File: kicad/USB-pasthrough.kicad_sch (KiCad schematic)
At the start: 93 parts, among them J1 USB_Power, J2 USB_C, J3 Cortex Debug, J4 Power_Sel, J5 SPI Display, J6 SWD, J7 USB_A, J8 MicroSD, SW1 Boot0, SW2 Reset, U1 AMS1117, U2 STM32F723VET6, Y1 8 MHz

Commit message: Tweak ID names, add serial port
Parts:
- added J?: Serial, Connector_PinHeader_2.54mm:PinHeader_1x03_P2.54mm_Vertical, symbol Connector_Generic:Conn_01x03
- renumbered ID5 to ID0, ID4 to ID1, ID3 to ID2, ID2 to ID3, ID1 to ID4
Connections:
- net GND: now also J?.3 (Pin_3)
- net TXD: now reaches U2.24 (PA2)
- net TXD: now also J?.1 (Pin_1)
- net RXD: now reaches U2.25 (PA3)
- net RXD: now also J?.2 (Pin_2)
- no-connect marks 49 -> 47
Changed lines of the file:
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@@
   (no_connect (at 132.08 160.02))
   (no_connect (at 181.61 105.41))
-  (no_connect (at 132.08 68.58))
   (no_connect (at 81.28 109.22))
   (no_connect (at 81.28 137.16))
   (no_connect (at 81.28 157.48))
-  (no_connect (at 132.08 66.04))
   (no_connect (at 81.28 134.62))
   (no_connect (at 81.28 142.24))
@@
     (effects (font (size 1.27 1.27)) (justify left bottom))
   )
+  (label "RXD" (at 163.83 144.78 180)
+    (effects (font (size 1.27 1.27)) (justify right bottom))
+  )
   (label "MMC1_CLK" (at 132.08 177.8 0)
     (effects (font (size 1.27 1.27)) (justify left bottom))
@@
     (effects (font (size 1.27 1.27)) (justify left bottom))
   )
+  (label "TXD" (at 132.08 66.04 0)
+    (effects (font (size 1.27 1.27)) (justify left bottom))
+  )
   (label "MMC1_CDET" (at 50.8 96.52 0)
     (effects (font (size 1.27 1.27)) (justify left bottom))
@@
     (effects (font (size 1.27 1.27)) (justify left bottom))
   )
+  (label "RXD" (at 132.08 68.58 0)
+    (effects (font (size 1.27 1.27)) (justify left bottom))
+  )
   (label "SWO" (at 184.15 93.98 180)
     (effects (font (size 1.27 1.27)) (justify right bottom))
@@
     (effects (font (size 1.27 1.27)) (justify right bottom))
   )
+  (label "TXD" (at 163.83 142.24 180)
+    (effects (font (size 1.27 1.27)) (justify right bottom))
+  )
   (label "USBC-" (at 207.01 149.86 180)
     (effects (font (size 1.27 1.27)) (justify right bottom))
@@
   (symbol (lib_id "Jumper:Jumper_2_Open") (at 76.2 121.92 0) (mirror y) (unit 1)
     (in_bom yes) (on_board yes)
-    (property "Reference" "ID4" (id 0) (at 76.2 120.65 0))
+    (property "Reference" "ID1" (id 0) (at 76.2 120.65 0))
     (property "Value" "Jumper_2_Bridged" (id 1) (at 76.2 118.11 0)
       (effects (font (size 1.27 1.27)) hide)
@@
   (symbol (lib_id "Jumper:Jumper_2_Bridged") (at 76.2 119.38 0) (mirror y) (unit 1)
     (in_bom yes) (on_board yes)
-    (property "Reference" "ID5" (id 0) (at 76.2 118.11 0))
+    (property "Reference" "ID0" (id 0) (at 76.2 118.11 0))
     (property "Value" "Jumper_2_Bridged" (id 1) (at 76.2 115.57 0)
       (effects (font (size 1.27 1.27)) hide)
@@
     (pin "99")
   )
+  (symbol (lib_id "power:GND") (at 163.83 147.32 0) (unit 1)
+    (in_bom yes) (on_board yes)
+    (property "Reference" "#PWR?" (id 0) (at 163.83 153.67 0)
+      (effects (font (size 1.27 1.27)) hide)
+    )
+    (property "Value" "GND" (id 1) (at 160.02 148.59 0))
+    (property "Footprint" "" (id 2) (at 163.83 147.32 0)
+      (effects (font (size 1.27 1.27)) hide)
+    )
+    (property "Datasheet" "" (id 3) (at 163.83 147.32 0)
+      (effects (font (size 1.27 1.27)) hide)
+    )
+    (pin "1")
+  )
   (symbol (lib_id "power:GND") (at 160.02 60.96 0) (unit 1)
     (in_bom yes) (on_board yes)
@@
     (pin "2")
   )
+  (symbol (lib_id "Connector_Generic:Conn_01x03") (at 168.91 144.78 0) (unit 1)
+    (in_bom yes) (on_board yes) (fields_autoplaced)
+    (property "Reference" "J?" (id 0) (at 171.45 143.5099 0)
+      (effects (font (size 1.27 1.27)) (justify left))
+    )
+    (property "Value" "Serial" (id 1) (at 171.45 146.0499 0)
+      (effects (font (size 1.27 1.27)) (justify left))
+    )
+    (property "Footprint" "Connector_PinHeader_2.54mm:PinHeader_1x03_P2.54mm_Vertical" (id 2) (at 168.91 144.78 0)
+      (effects (font (size 1.27 1.27)) hide)
+    )
+    (property "Datasheet" "~" (id 3) (at 168.91 144.78 0)
+      (effects (font (size 1.27 1.27)) hide)
+    )
+    (pin "1")
+    (pin "2")
+    (pin "3")
+  )
   (symbol (lib_id "power:PWR_FLAG") (at 45.72 27.94 0) (unit 1)
     (in_bom yes) (on_board yes) (fields_autoplaced)
@@
   (symbol (lib_id "Jumper:Jumper_2_Bridged") (at 76.2 127 0) (mirror y) (unit 1)
     (in_bom yes) (on_board yes)
-    (property "Reference" "ID2" (id 0) (at 76.2 125.73 0))
+    (property "Reference" "ID3" (id 0) (at 76.2 125.73 0))
     (property "Value" "Jumper_2_Bridged" (id 1) (at 76.2 123.19 0)
       (effects (font (size 1.27 1.27)) hide)
@@
   (symbol (lib_id "Jumper:Jumper_2_Bridged") (at 76.2 124.46 0) (mirror y) (unit 1)
     (in_bom yes) (on_board yes)
-    (property "Reference" "ID3" (id 0) (at 76.2 123.19 0))
+    (property "Reference" "ID2" (id 0) (at 76.2 123.19 0))
     (property "Value" "Jumper_2_Bridged" (id 1) (at 76.2 120.65 0)
       (effects (font (size 1.27 1.27)) hide)
@@
   (symbol (lib_id "Jumper:Jumper_2_Bridged") (at 76.2 129.54 0) (mirror y) (unit 1)
     (in_bom yes) (on_board yes)
-    (property "Reference" "ID1" (id 0) (at 76.2 128.27 0))
+    (property "Reference" "ID4" (id 0) (at 76.2 128.27 0))
     (property "Value" "Jumper_2_Bridged" (id 1) (at 76.2 125.73 0)
       (effects (font (size 1.27 1.27)) hide)
@@
       (reference "#PWR0108") (unit 1) (value "GND") (footprint "")
     )
+    (path "/2bf153cc-e448-4386-8752-8ba0ab506fbf"
+      (reference "#PWR?") (unit 1) (value "GND") (footprint "")
+    )
     (path "/17fb6d59-e121-4e89-9918-78c9648a257a"
       (reference "C1") (unit 1) (value "10uF") (footprint "Capacitor_THT:CP_Radial_D5.0mm_P2.50mm")
@@
       (reference "H4") (unit 1) (value "MountingHole") (footprint "MountingHole:MountingHole_2.2mm_M2_Pad")
     )
-    (path "/95c1312c-0851-4fe5-a936-d7533c7cbaf8"
-      (reference "ID1") (unit 1) (value "Jumper_2_Bridged") (footprint "Jumper:SolderJumper-2_P1.3mm_Bridged_Pad1.0x1.5mm")
+    (path "/1858f103-0550-4454-a9a8-cb3c44998e1e"
+      (reference "ID0") (unit 1) (value "Jumper_2_Bridged") (footprint "Jumper:SolderJumper-2_P1.3mm_Bridged_Pad1.0x1.5mm")
     )
-    (path "/8b9373f4-2597-4d9f-8245-62eb92cb212f"
-      (reference "ID2") (unit 1) (value "Jumper_2_Bridged") (footprint "Jumper:SolderJumper-2_P1.3mm_Bridged_Pad1.0x1.5mm")
+    (path "/1586b523-a3cf-43e8-bf9d-0533c598fcc1"
+      (reference "ID1") (unit 1) (value "Jumper_2_Bridged") (footprint "Jumper:SolderJumper-2_P1.3mm_Open_Pad1.0x1.5mm")
     )
     (path "/8d554622-7ff9-41d4-a107-16b60e1fce82"
-      (reference "ID3") (unit 1) (value "Jumper_2_Bridged") (footprint "Jumper:SolderJumper-2_P1.3mm_Bridged_Pad1.0x1.5mm")
+      (reference "ID2") (unit 1) (value "Jumper_2_Bridged") (footprint "Jumper:SolderJumper-2_P1.3mm_Bridged_Pad1.0x1.5mm")
     )
-    (path "/1586b523-a3cf-43e8-bf9d-0533c598fcc1"
-      (reference "ID4") (unit 1) (value "Jumper_2_Bridged") (footprint "Jumper:SolderJumper-2_P1.3mm_Open_Pad1.0x1.5mm")
+    (path "/8b9373f4-2597-4d9f-8245-62eb92cb212f"
+      (reference "ID3") (unit 1) (value "Jumper_2_Bridged") (footprint "Jumper:SolderJumper-2_P1.3mm_Bridged_Pad1.0x1.5mm")
     )
-    (path "/1858f103-0550-4454-a9a8-cb3c44998e1e"
-      (reference "ID5") (unit 1) (value "Jumper_2_Bridged") (footprint "Jumper:SolderJumper-2_P1.3mm_Bridged_Pad1.0x1.5mm")
+    (path "/95c1312c-0851-4fe5-a936-d7533c7cbaf8"
+      (reference "ID4") (unit 1) (value "Jumper_2_Bridged") (footprint "Jumper:SolderJumper-2_P1.3mm_Bridged_Pad1.0x1.5mm")
     )
     (path "/7cf7e8fc-d4c5-4161-b905-d74139026239"
@@
       (reference "J8") (unit 1) (value "MicroSD") (footprint "Connector_Card:microSD_HC_Hirose_DM3AT-SF-PEJM5")
     )
+    (path "/5e2d672b-5bf9-4abe-ba7e-647e105a370c"
+      (reference "J?") (unit 1) (value "Serial") (footprint "Connector_PinHeader_2.54mm:PinHeader_1x03_P2.54mm_Vertical")
+    )
     (path "/97339053-1ba0-429b-8e6a-4e4aa25ddc74"

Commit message: Start switching to Full Sized SD socket
The uSD socket is too small, use bigger socket for easier
soldering.
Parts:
- added J?: SD_Card, symbol Connector:SD_Card
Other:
- moved on the sheet: J?
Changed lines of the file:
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@@
     (effects (font (size 1.27 1.27)) (justify left bottom))
   )
-  (label "RXD" (at 163.83 144.78 180)
+  (label "RXD" (at 30.48 133.35 180)
     (effects (font (size 1.27 1.27)) (justify right bottom))
   )
@@
     (effects (font (size 1.27 1.27)) (justify right bottom))
   )
-  (label "TXD" (at 163.83 142.24 180)
+  (label "TXD" (at 30.48 130.81 180)
     (effects (font (size 1.27 1.27)) (justify right bottom))
   )
@@
     (pin "99")
   )
-  (symbol (lib_id "power:GND") (at 163.83 147.32 0) (unit 1)
+  (symbol (lib_id "power:GND") (at 30.48 135.89 0) (unit 1)
     (in_bom yes) (on_board yes)
-    (property "Reference" "#PWR?" (id 0) (at 163.83 153.67 0)
+    (property "Reference" "#PWR?" (id 0) (at 30.48 142.24 0)
       (effects (font (size 1.27 1.27)) hide)
     )
-    (property "Value" "GND" (id 1) (at 160.02 148.59 0))
-    (property "Footprint" "" (id 2) (at 163.83 147.32 0)
+    (property "Value" "GND" (id 1) (at 26.67 137.16 0))
+    (property "Footprint" "" (id 2) (at 30.48 135.89 0)
       (effects (font (size 1.27 1.27)) hide)
     )
-    (property "Datasheet" "" (id 3) (at 163.83 147.32 0)
+    (property "Datasheet" "" (id 3) (at 30.48 135.89 0)
       (effects (font (size 1.27 1.27)) hide)
     )
@@
     (pin "2")
   )
-  (symbol (lib_id "Connector_Generic:Conn_01x03") (at 168.91 144.78 0) (unit 1)
+  (symbol (lib_id "Connector_Generic:Conn_01x03") (at 35.56 133.35 0) (unit 1)
     (in_bom yes) (on_board yes) (fields_autoplaced)
-    (property "Reference" "J?" (id 0) (at 171.45 143.5099 0)
+    (property "Reference" "J?" (id 0) (at 38.1 132.0799 0)
       (effects (font (size 1.27 1.27)) (justify left))
     )
-    (property "Value" "Serial" (id 1) (at 171.45 146.0499 0)
+    (property "Value" "Serial" (id 1) (at 38.1 134.6199 0)
       (effects (font (size 1.27 1.27)) (justify left))
     )
-    (property "Footprint" "Connector_PinHeader_2.54mm:PinHeader_1x03_P2.54mm_Vertical" (id 2) (at 168.91 144.78 0)
+    (property "Footprint" "Connector_PinHeader_2.54mm:PinHeader_1x03_P2.54mm_Vertical" (id 2) (at 35.56 133.35 0)
       (effects (font (size 1.27 1.27)) hide)
     )
-    (property "Datasheet" "~" (id 3) (at 168.91 144.78 0)
+    (property "Datasheet" "~" (id 3) (at 35.56 133.35 0)
       (effects (font (size 1.27 1.27)) hide)
     )
@@
     (pin "2")
   )
+  (symbol (lib_id "Connector:SD_Card") (at 168.91 143.51 0) (unit 1)
+    (in_bom yes) (on_board yes) (fields_autoplaced)
+    (property "Reference" "J?" (id 0) (at 168.91 125.73 0))
+    (property "Value" "SD_Card" (id 1) (at 168.91 128.27 0))
+    (property "Footprint" "" (id 2) (at 168.91 143.51 0)
+      (effects (font (size 1.27 1.27)) hide)
+    )
+    (property "Datasheet" "http://portal.fciconnect.com/Comergent//fci/drawing/10067847.pdf" (id 3) (at 168.91 143.51 0)
+      (effects (font (size 1.27 1.27)) hide)
+    )
+    (pin "1")
+    (pin "10")
+    (pin "11")
+    (pin "12")
+    (pin "13")
+    (pin "2")
+    (pin "3")
+    (pin "4")
+    (pin "5")
+    (pin "6")
+    (pin "7")
+    (pin "8")
+    (pin "9")
+  )
   (symbol (lib_name "MountingHole_3") (lib_id "Mechanical:MountingHole") (at 20.32 80.01 0) (unit 1)
     (in_bom yes) (on_board yes) (fields_autoplaced)
@@
       (reference "J?") (unit 1) (value "Serial") (footprint "Connector_PinHeader_2.54mm:PinHeader_1x03_P2.54mm_Vertical")
     )
+    (path "/aa5a7d34-f533-44f1-a357-de5c629aef10"
+      (reference "J?") (unit 1) (value "SD_Card") (footprint "")
+    )
     (path "/97339053-1ba0-429b-8e6a-4e4aa25ddc74"

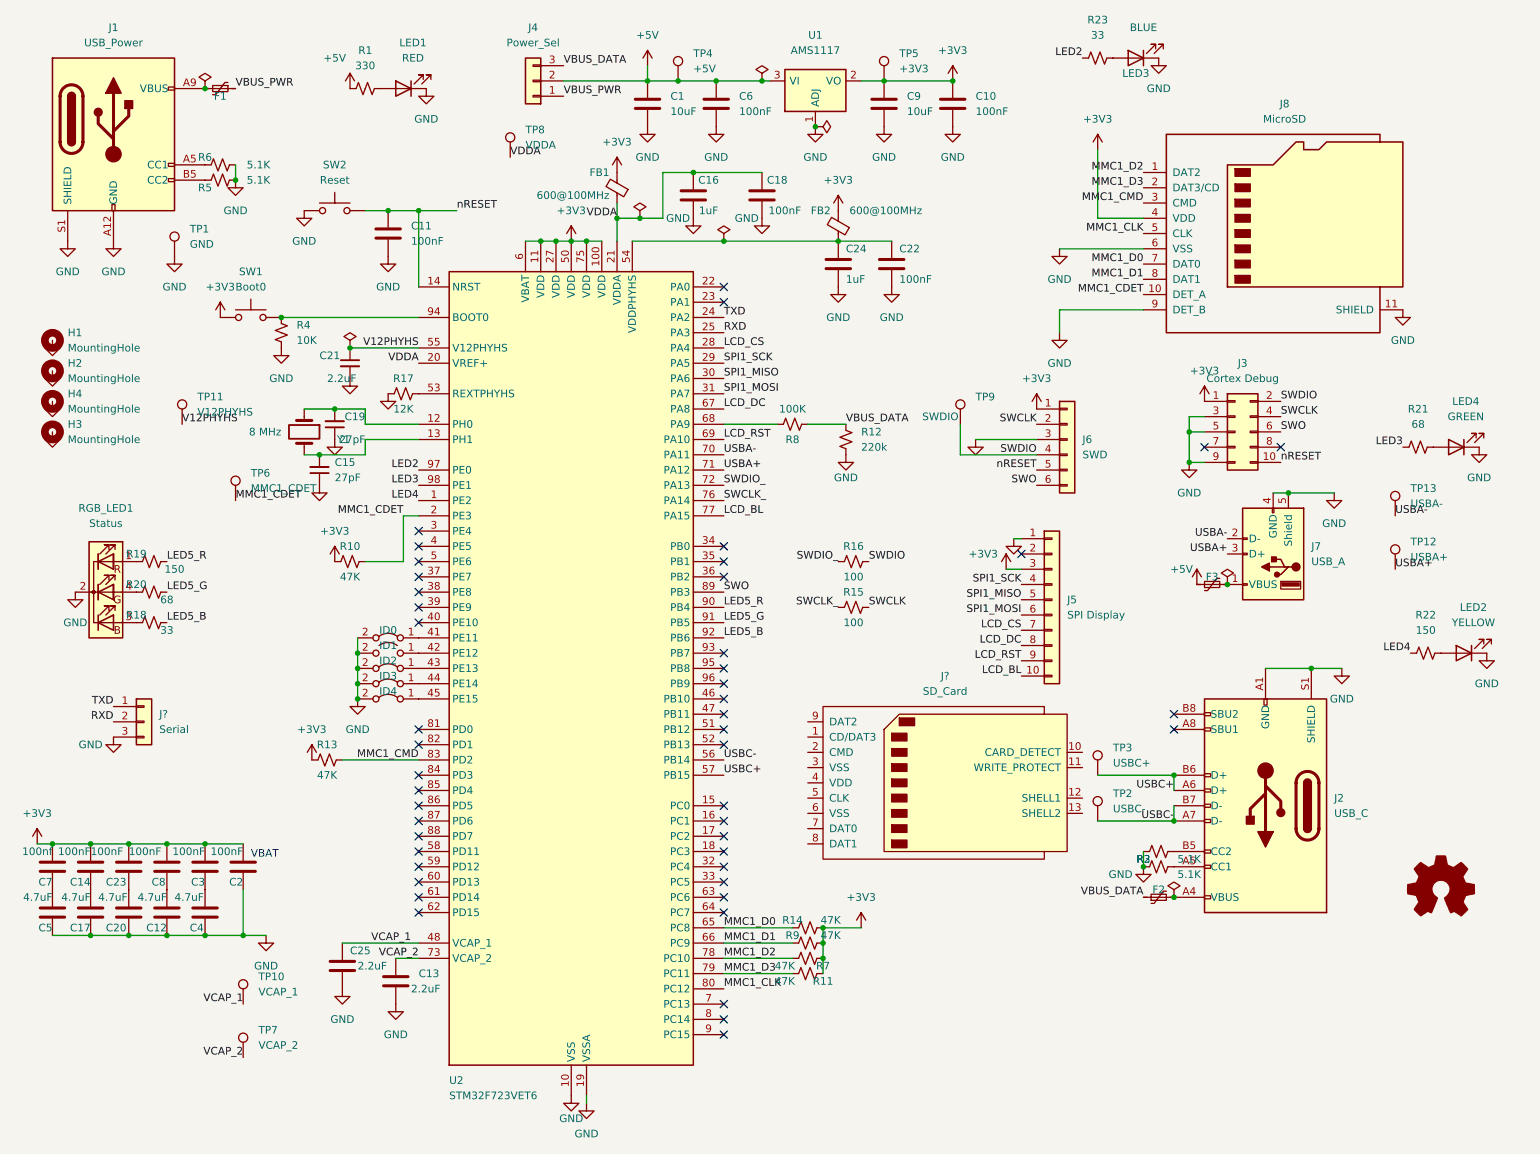
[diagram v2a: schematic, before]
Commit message: Add fulsized SD Card connector serial etc...
Add KiCad symbol and footprint for SD Card connector to try out
overlaying Full size and uSD connectors allowing support for either
one depending on which connector is installed.

Also add SMD USB A connector for possible use in place of THT.
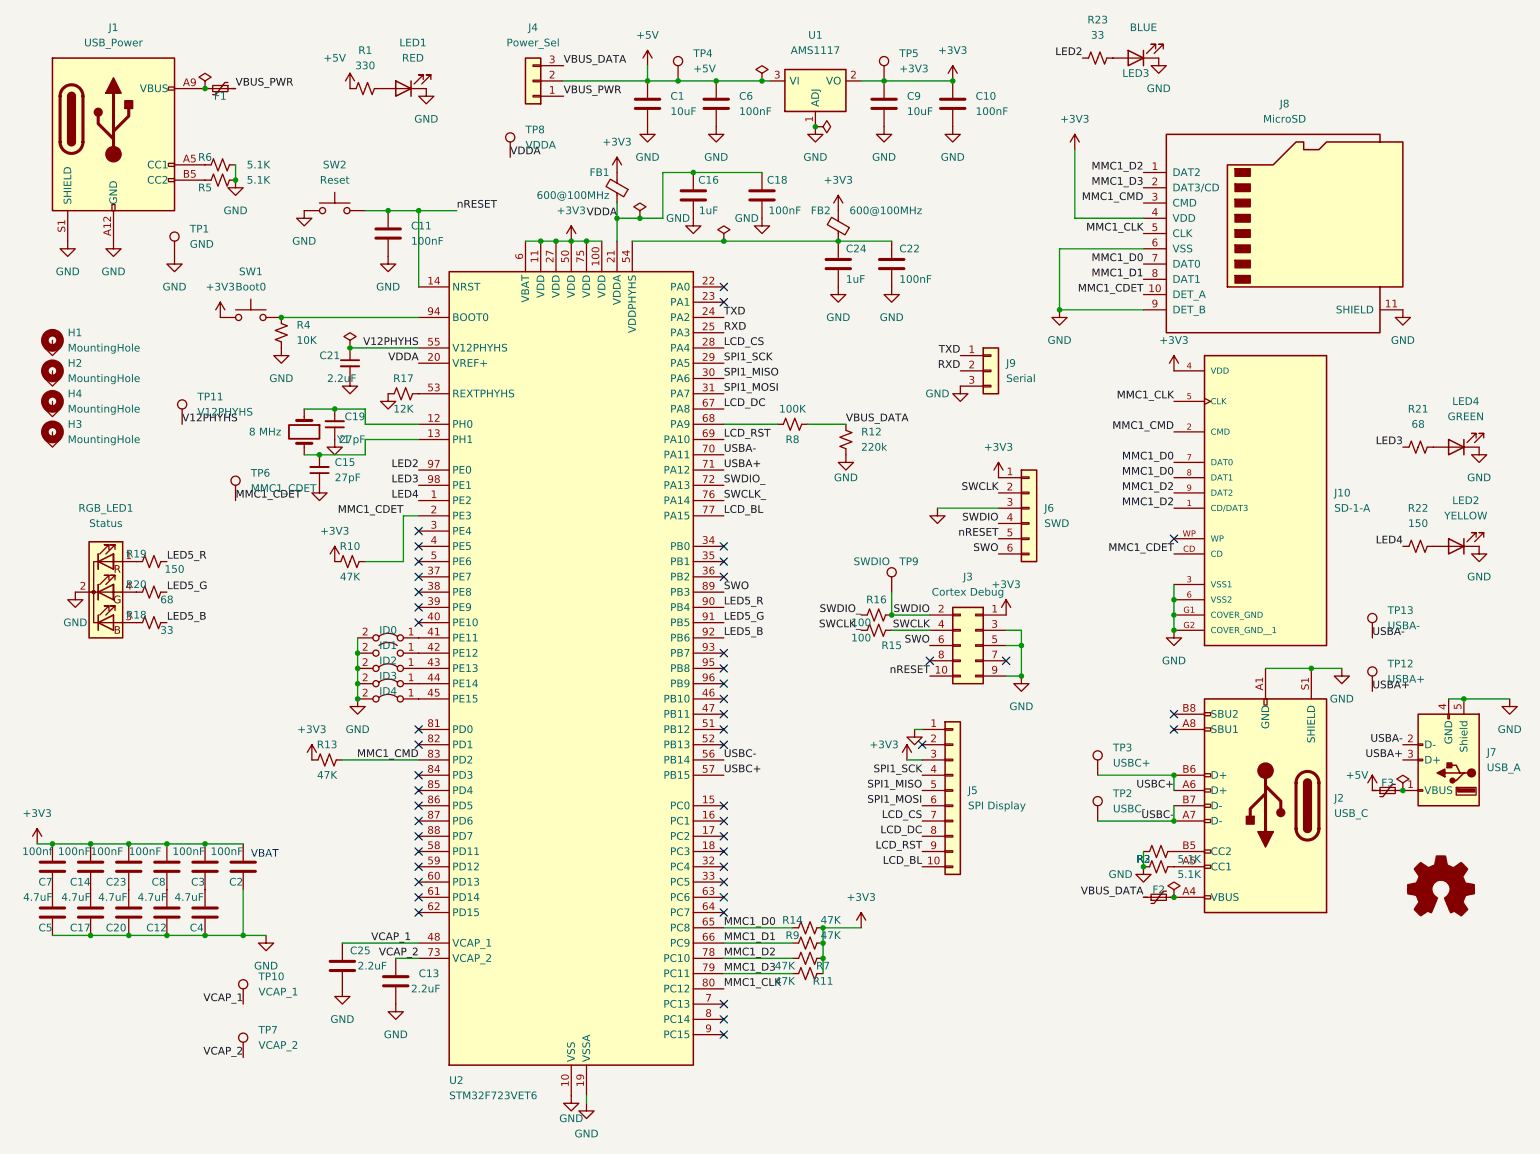
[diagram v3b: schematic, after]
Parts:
- removed J?: SD_Card, symbol Connector:SD_Card
- added J10: SD-1-A, SD-1-A:CUI_SD-1-A, symbol SD-1-A:SD-1-A
- gave numbers to parts that had none: 1
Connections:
- net +3V3: now also J10.4 (VDD)
- net GND: now also J10.3 (VSS1), J10.6 (VSS2), J10.G1 (COVER_GND), J10.G2 (COVER_GND__1)
- net MMC1_CDET: now also J10.CD
- net MMC1_CLK: now also J10.5 (CLK)
- net MMC1_CMD: now also J10.2 (CMD)
- net MMC1_D0: now also J10.7 (DAT0), J10.8 (DAT1)
- net MMC1_D2: now also J10.1 (CD/DAT3), J10.9 (DAT2)
- no-connect marks 47 -> 48
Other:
- moved on the sheet: F3, J3, J5, J6, J7, J9, LED2, R15, R16, R22, TP12, TP13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
